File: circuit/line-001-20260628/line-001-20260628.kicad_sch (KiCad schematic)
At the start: 220 parts, among them J1 Conn_01x02_Pin, J2 Conn_01x02_Pin, J3 ICSP, J4 USB_C_Receptacle_USB2.0_16P, Q1 Q_Photo_NPN_CE, Q10 Q_Photo_NPN_CE, Q11 Q_Photo_NPN_CE, Q12 Q_Photo_NPN_CE, Q13 Q_Photo_NPN_CE, Q14 Q_Photo_NPN_CE, Q15 Q_Photo_NPN_CE, Q16 Q_Photo_NPN_CE, Q17 Q_Photo_NPN_CE, Q18 Q_Photo_NPN_CE, Q19 Q_Photo_NPN_CE, Q2 Q_Photo_NPN_CE, Q20 Q_Photo_NPN_CE, Q21 Q_Photo_NPN_CE, Q22 Q_Photo_NPN_CE, Q23 Q_Photo_NPN_CE, Q24 Q_Photo_NPN_CE, Q25 Q_Photo_NPN_CE, Q26 Q_Photo_NPN_CE, Q27 Q_Photo_NPN_CE, Q28 Q_Photo_NPN_CE, Q29 Q_Photo_NPN_CE, Q3 Q_Photo_NPN_CE, Q30 Q_Photo_NPN_CE, Q31 Q_Photo_NPN_CE, Q32 Q_Photo_NPN_CE, Q37 Q_Photo_NPN_CE, Q38 Q_Photo_NPN_CE, Q39 Q_Photo_NPN_CE, Q4 Q_Photo_NPN_CE, Q40 Q_Photo_NPN_CE, Q5 Q_Photo_NPN_CE, Q6 Q_Photo_NPN_CE, Q7 Q_Photo_NPN_CE, Q8 Q_Photo_NPN_CE, Q9 Q_Photo_NPN_CE, SW1 SW_Push, SW2 SW_SPDT, U1 LM393DR, U10 LM393DR, U11 LM393DR, U12 LM393DR, U13 LM393DR, U14 LM393DR, U15 LM393DR, U16 LM393DR, U17 ATmega2560-16A, U18 CH340G, U2 LM393DR, U3 LM393DR, U4 LM393DR, U5 LM393DR, U6 LM393DR, U7 LM393DR, U8 LM393DR, U9 LM393DR, Y1 16MHz, Y2 12MHz

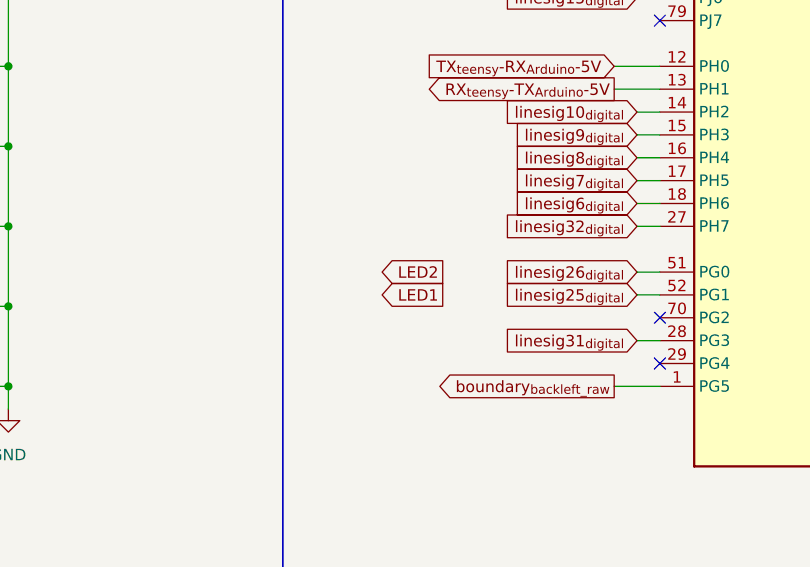
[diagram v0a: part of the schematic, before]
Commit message: Update ラインセンサ基板にGNDビアを打った
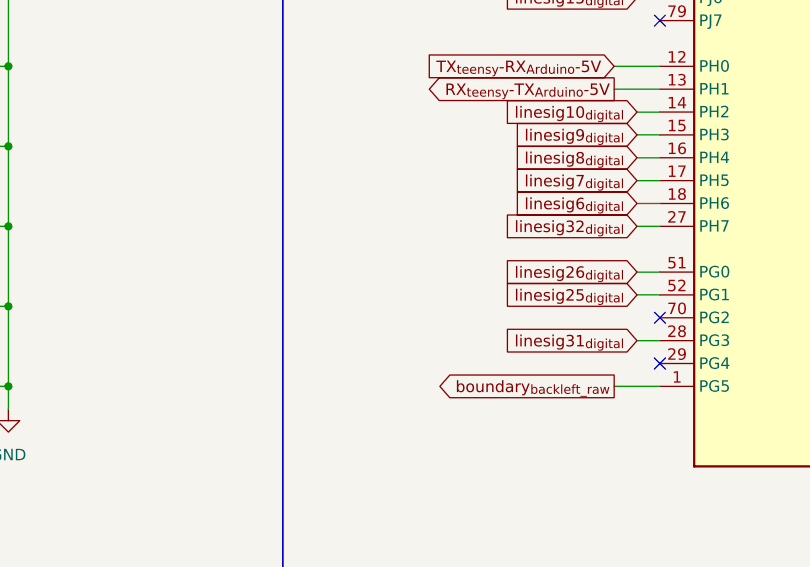
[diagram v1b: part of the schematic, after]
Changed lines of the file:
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@@
-		)
-	)
-	(global_label "LED2"
-		(shape output)
-		(at 297.18 156.21 180)
-		(fields_autoplaced yes)
-		(effects
-			(font
-				(size 1.27 1.27)
-			)
-			(justify right)
-		)
-		(property "Intersheetrefs" "${INTERSHEET_REFS}"
-			(at 289.9741 156.21 0)
-			(hide yes)
-			(show_name no)
-			(do_not_autoplace no)
-			(effects
-				(font
-					(size 1.27 1.27)
-				)
-				(justify right)
-			)
 		)
 	)
@@
 			)
 		)
-	)
-	(global_label "LED1"
-		(shape output)
-		(at 297.18 158.75 180)
-		(fields_autoplaced yes)
-		(effects
-			(font
-				(size 1.27 1.27)
-			)
-			(justify right)
-		)
-		(property "Intersheetrefs" "${INTERSHEET_REFS}"
-			(at 289.9741 158.75 0)
-			(hide yes)
-			(show_name no)
-			(do_not_autoplace no)
-			(effects
-				(font
-					(size 1.27 1.27)
-				)
-				(justify right)
-			)
-		)

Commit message: Update ラインセンサ基板の回路図とボード図を更新
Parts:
- C21, C22, C26, C27: value C -> 10u
- R83, R84, R87, R88: value R -> 1K
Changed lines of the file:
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@@
 			)
 		)
-		(property "Value" "C"
+		(property "Value" "10u"
 			(at 430.53 289.56 0)
 			(show_name no)
@@
 			)
 		)
-		(property "Value" "C"
+		(property "Value" "10u"
 			(at 430.53 269.24 0)
 			(show_name no)
@@
 			)
 		)
-		(property "Value" "C"
+		(property "Value" "10u"
 			(at 358.14 289.56 0)
 			(show_name no)
@@
 			)
 		)
-		(property "Value" "R"
+		(property "Value" "1K"
 			(at 345.44 278.13 90)
 			(show_name no)
@@
 			)
 		)
-		(property "Value" "R"
+		(property "Value" "1K"
 			(at 417.83 257.81 90)
 			(show_name no)
@@
 			)
 		)
-		(property "Value" "C"
+		(property "Value" "10u"
 			(at 358.14 269.24 0)
 			(show_name no)
@@
 			)
 		)
-		(property "Value" "R"
+		(property "Value" "1K"
 			(at 417.83 278.13 90)
 			(show_name no)
@@
 			)
 		)
-		(property "Value" "R"
+		(property "Value" "1K"
 			(at 345.44 257.81 90)
 			(show_name no)

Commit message: Update ラインセンサのサイドのコンパレータを追加
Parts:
- added C23, C24: 100n, Capacitor_SMD:C_0805_2012Metric, symbol Device:C_Small
- added U19, U20: LM393DR, Package_SO:SOIC-8_3.9x4.9mm_P1.27mm, symbol @Thrive_symbol_line:LM393DR
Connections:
- net +5VD: now also C23.2, C24.2, U19.8 (V_{CC}), U20.8 (V_{CC})
- net GND: now also C23.1, C24.1, U19.4 (GND), U20.4 (GND)
- net boundary_{frontleft}: now also U20.2 (1_{IN-})
- net boundary_{frontright}: now also U19.2 (1_{IN-})
- net linesig1^{side}_{raw}: now also U19.3 (1_{IN+})
- net linesig2^{side}_{raw}: now also U20.3 (1_{IN+})
- net linesig2^{side}_{digital}: now reaches U17.50 (PD7)
- net linesig2^{side}_{digital}: now also U20.1 (1_{OUT})
- net linesig1^{side}_{digital}: now reaches U17.95 (PF2)
- net linesig1^{side}_{digital}: now also U19.1 (1_{OUT})
- no-connect marks 49 -> 53
